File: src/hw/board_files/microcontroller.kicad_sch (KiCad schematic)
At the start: 15 parts, among them Q3 PMOS, Q4 NMOS, U6 ESP32-S3-WROOM-1, Y1 32.768kHz

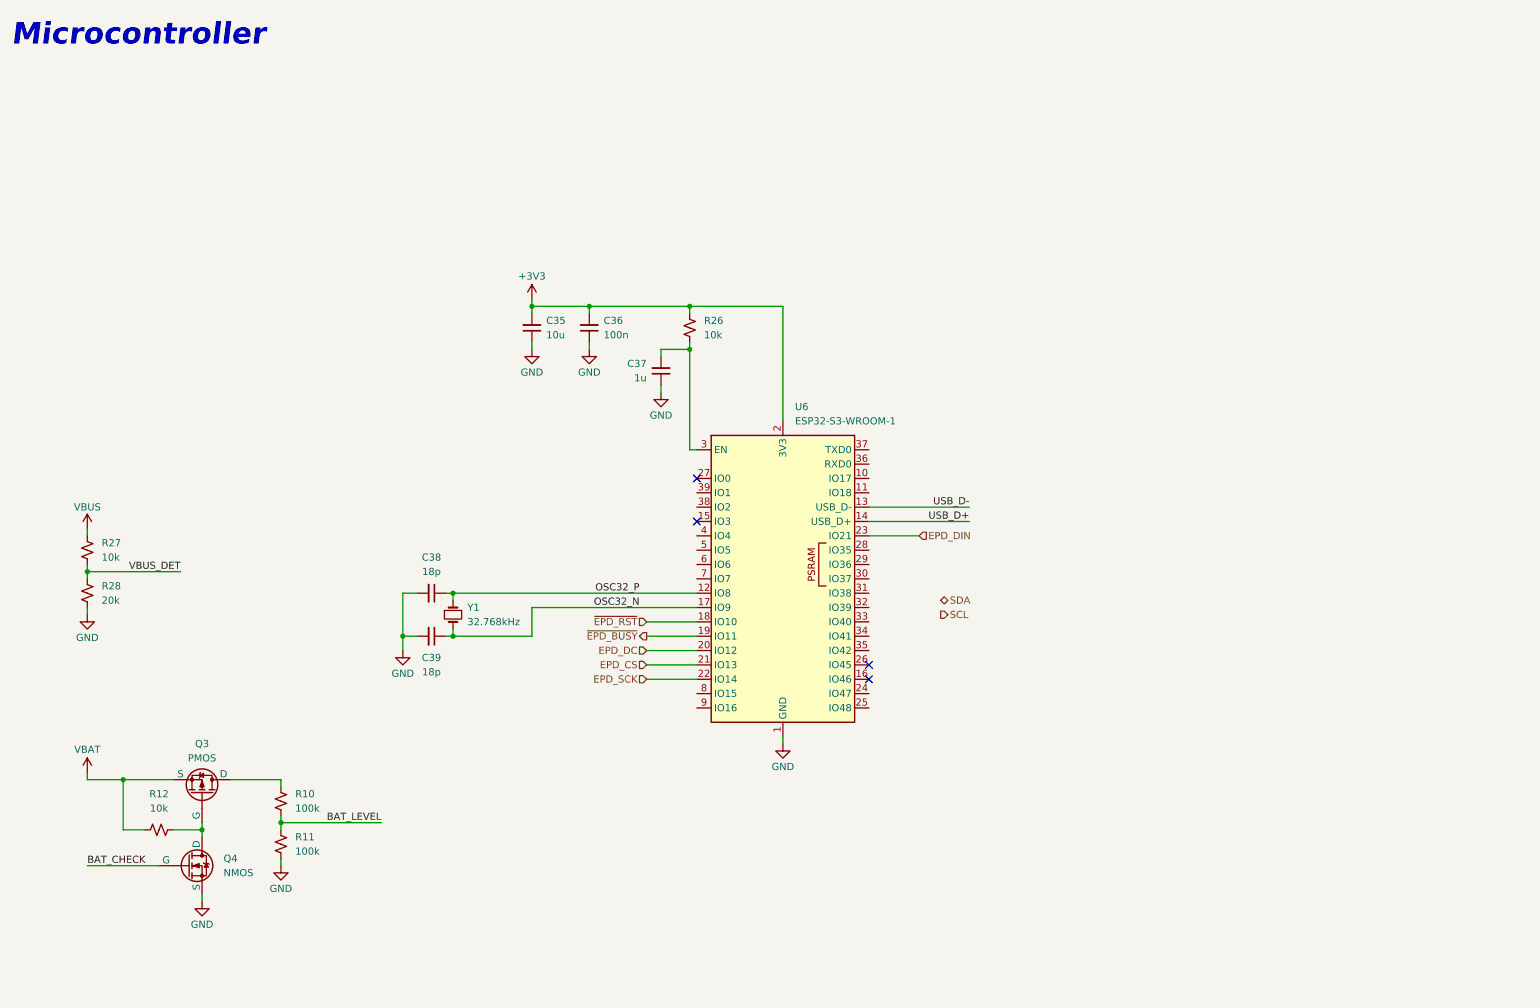
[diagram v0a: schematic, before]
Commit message: Schematic almost done. Assigning footprints
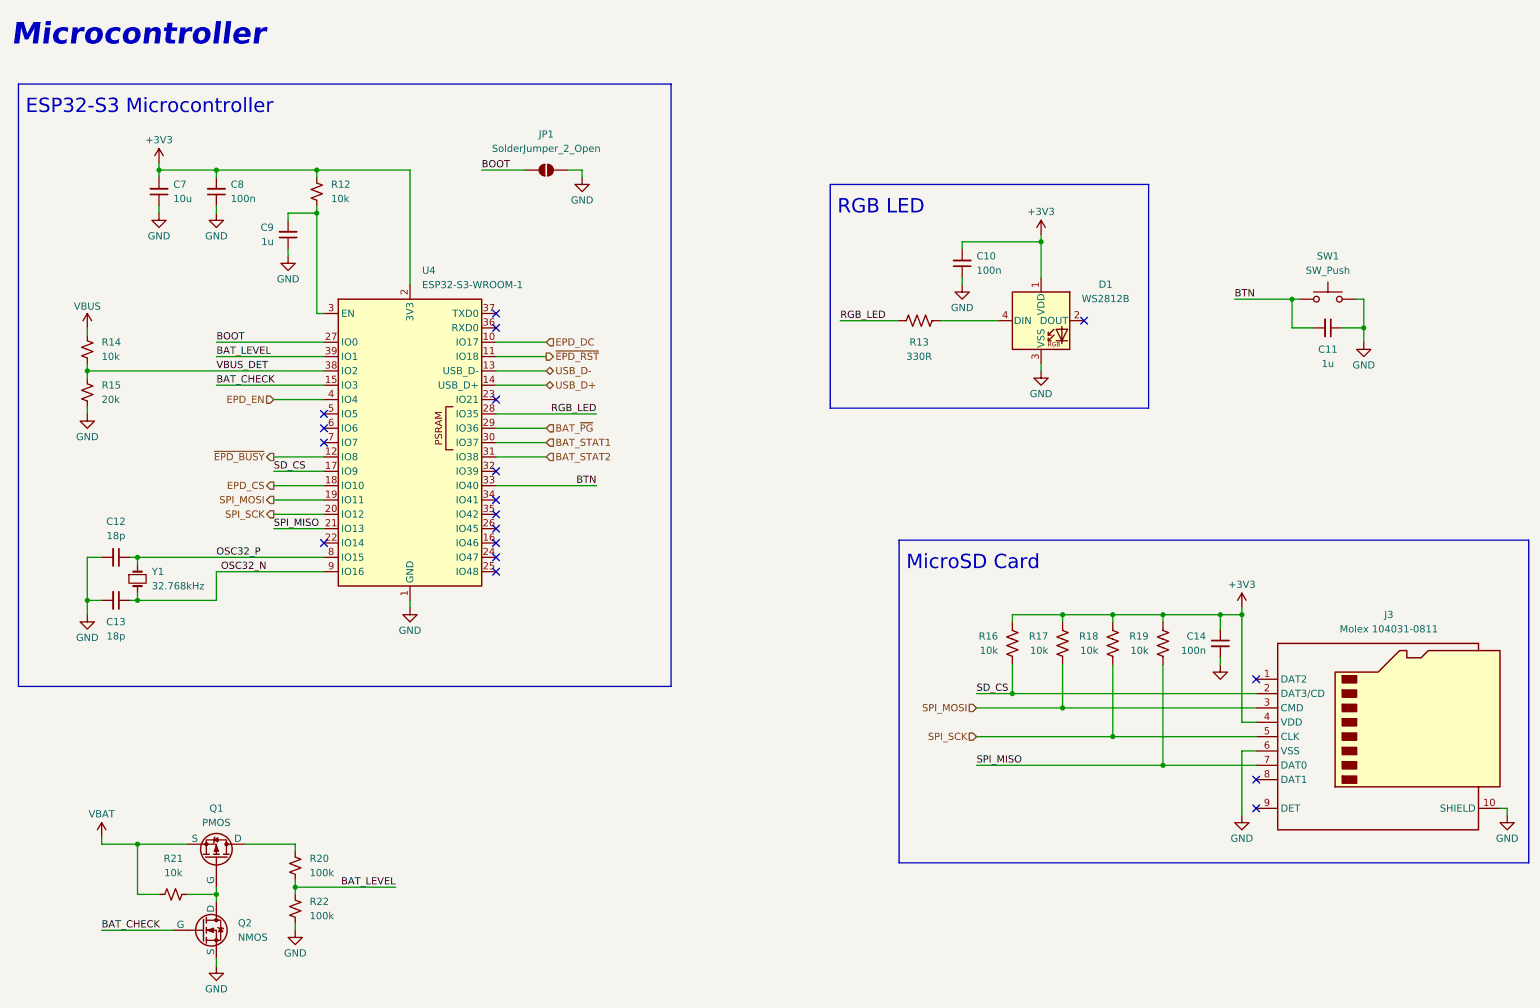
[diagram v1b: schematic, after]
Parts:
- added C10, C14: 100n, Capacitor_SMD:C_0603_1608Metric_Pad1.08x0.95mm_HandSolder, symbol Device:C_Small
- added C11: 1u, Capacitor_SMD:C_0603_1608Metric_Pad1.08x0.95mm_HandSolder, symbol Device:C_Small
- added D1: WS2812B, LED_SMD:LED_WS2812B_PLCC4_5.0x5.0mm_P3.2mm, symbol LED:WS2812B
- added J3: Molex 104031-0811, Connector_Card:microSD_HC_Molex_104031-0811, symbol Connector:Micro_SD_Card_Det1
- added JP1: SolderJumper_2_Open, Jumper:SolderJumper-2_P1.3mm_Open_RoundedPad1.0x1.5mm, symbol Jumper:SolderJumper_2_Open
- added R13: 330R, symbol Device:R_US
- added R16, R17, R18, R19: 10k, Resistor_SMD:R_0603_1608Metric_Pad0.98x0.95mm_HandSolder, symbol Device:R_US
- added SW1: SW_Push, Button_Switch_THT:SW_PUSH_6mm, symbol Switch:SW_Push
- renumbered C38 to C12, C39 to C13, C35 to C7, C36 to C8, C37 to C9, Q3 to Q1, Q4 to Q2, R26 to R12, R27 to R14, R28 to R15, R10 to R20, R12 to R21, R11 to R22, U6 to U4
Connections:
- net +3V3: now also C10.2, C14.1, D1.1 (VDD), J3.4 (VDD), R16.1, R17.1, R18.1, R19.1
- net BAT_CHECK: now also U4.15 (IO3)
- net BAT_LEVEL: now also U4.39 (IO1)
- net EPD_CS: now also U4.18 (IO10); no longer U4.21 (IO13)
- net EPD_DC: now also U4.10 (IO17); no longer U4.20 (IO12)
- net GND: now also C10.1, C11.1, C14.2, D1.3 (VSS), J3.10 (SHIELD), J3.6 (VSS), JP1.2 (B), SW1.2
- net OSC32_N: now also U4.9 (IO16); no longer U4.17 (IO9)
- net OSC32_P: now also U4.8 (IO15); no longer U4.12 (IO8)
- net VBUS_DET: now also U4.38 (IO2)
- net ~{EPD_BUSY}: now also U4.12 (IO8); no longer U4.19 (IO11)
- net ~{EPD_RST}: now also U4.11 (IO18); no longer U4.18 (IO10)
- net BOOT: now reaches U4.27 (IO0)
- net BOOT: now also JP1.1 (A)
- net RGB_LED: now reaches U4.28 (IO35)
- net RGB_LED: now also R13.1
- net BAT_~{PG}: now reaches U4.29 (IO36)
- net BAT_STAT1: now reaches U4.30 (IO37)
- net BAT_STAT2: now reaches U4.31 (IO38)
- net BTN: now reaches U4.33 (IO40)
- net BTN: now also C11.2, SW1.1
- net EPD_EN: now reaches U4.4 (IO4)
- net EPD_DIN: no longer names the net of U4.23 (IO21)
- net EPD_SCK: no longer names the net of U4.22 (IO14)
- new net: D1.4 (DIN), R13.2
- new net SD_CS: J3.2 (DAT3/CD), R16.2, U4.17 (IO9)
- new net SPI_MISO: J3.7 (DAT0), R19.2, U4.21 (IO13)
- new net SPI_MOSI: J3.3 (CMD), R17.2, U4.19 (IO11)
- new net SPI_SCK: J3.5 (CLK), R18.2, U4.20 (IO12)
- no-connect marks 4 -> 18
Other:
- note added: "ESP32-S3 Microcontroller"
- note added: "MicroSD Card"
- note added: "RGB LED"
- moved on the sheet: C12, C13, C7, C8, C9, Q1, Q2, R12, R14, R15, R20, R21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

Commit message: Schematic done. Started layout
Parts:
- removed Q1: PMOS, symbol Simulation_SPICE:PMOS
- removed Q2: NMOS, symbol Simulation_SPICE:NMOS
- added C12, C13: 1u, Capacitor_SMD:C_0603_1608Metric_Pad1.08x0.95mm_HandSolder, symbol Device:C_Small
- added C17: 100n, Capacitor_SMD:C_0603_1608Metric_Pad1.08x0.95mm_HandSolder, symbol Device:C_Small
- added J4: Conn_01x10, Connector_PinSocket_2.54mm:PinSocket_1x10_P2.54mm_Horizontal, symbol Connector_Generic:Conn_01x10
- added Q1: AO3401A, Package_TO_SOT_SMD:SOT-23, symbol Transistor_FET:AO3401A
- added Q2: BSS138, Package_TO_SOT_SMD:SOT-23, symbol Transistor_FET:BSS138
- added SW2, SW3: SW_Push, Button_Switch_THT:SW_PUSH_6mm, symbol Switch:SW_Push
- R12, R13, R14, R15, R21: footprint (none) -> Resistor_SMD:R_0603_1608Metric_Pad0.98x0.95mm_HandSolder
- R20, R22: footprint (none) -> Resistor_SMD:R_0805_2012Metric_Pad1.20x1.40mm_HandSolder
- renumbered C9 to C10, C10 to C11, C12 to C14, C13 to C15, C14 to C16, C11 to C9
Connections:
- net +3V3: now also J4.1 (Pin_1)
- net BAT_CHECK: now also Q2.1 (G)
- net EPD_CS: now also J4.6 (Pin_6)
- net GND: now also C12.1, C13.1, C17.1, J4.10 (Pin_10), Q2.2 (S), SW2.2, SW3.2
- net SD_CS: now also J4.5 (Pin_5)
- net SPI_MISO: now also J4.2 (Pin_2)
- net SPI_MOSI: now also J4.3 (Pin_3)
- net SPI_SCK: now also J4.4 (Pin_4)
- net VBAT: now also C17.2, Q1.2 (S)
- net GPIO41: now reaches U4.34 (IO41)
- net GPIO41: now also J4.8 (Pin_8)
- net GPIO42: now reaches U4.35 (IO42)
- net GPIO42: now also J4.9 (Pin_9)
- net BTN_1: now reaches U4.5 (IO5)
- net BTN_1: now also C9.2, SW1.1
- net BTN_2: now reaches U4.6 (IO6)
- net BTN_2: now also C12.2, SW2.1
- net BTN_3: now reaches U4.7 (IO7)
- net BTN_3: now also C13.2, SW3.1
- net at R20.1: now also Q1.3 (D)
- net at R21.2: now also Q1.1 (G), Q2.3 (D)
- removed net BTN: C9.2, SW1.1, U4.33 (IO40)
- new net GPIO40: J4.7 (Pin_7), U4.33 (IO40)
- no-connect marks 18 -> 13
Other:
- moved on the sheet: C9, SW1

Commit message: Laid out main components
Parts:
- J3: footprint Connector_Card:microSD_HC_Molex_104031-0811 -> Connector_Card:microSD_HC_Hirose_DM3D-SF
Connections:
- net BAT_STAT1: now also U4.24 (IO47); no longer U4.30 (IO37)
- net BAT_STAT2: now also U4.25 (IO48); no longer U4.31 (IO38)
- net BAT_~{PG}: now also U4.23 (IO21); no longer U4.29 (IO36)
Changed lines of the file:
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@@
-	)
-	(no_connect
-		(at 99.06 111.76)
-	)
-	(no_connect
-		(at 99.06 81.28)
-	)
-	(no_connect
-		(at 99.06 109.22)
 	)
 	(no_connect
@@
 		(at 203.2 67.31)
 	)
+	(no_connect
+		(at 99.06 86.36)
+	)
+	(no_connect
+		(at 99.06 91.44)
+	)
+	(no_connect
+		(at 99.06 88.9)
+	)
 	(wire
 		(pts
@@
 	(wire
 		(pts
-			(xy 107.95 91.44) (xy 99.06 91.44)
+			(xy 107.95 111.76) (xy 99.06 111.76)
 		)
 		(stroke
@@
 	(wire
 		(pts
-			(xy 107.95 86.36) (xy 99.06 86.36)
+			(xy 107.95 81.28) (xy 99.06 81.28)
 		)
 		(stroke
@@
 	(wire
 		(pts
-			(xy 107.95 88.9) (xy 99.06 88.9)
+			(xy 107.95 109.22) (xy 99.06 109.22)
 		)
 		(stroke
@@
 	(hierarchical_label "BAT_STAT1"
 		(shape input)
-		(at 107.95 88.9 0)
+		(at 107.95 109.22 0)
 		(effects
 			(font
@@
 	(hierarchical_label "BAT_~{PG}"
 		(shape input)
-		(at 107.95 86.36 0)
+		(at 107.95 81.28 0)
 		(effects
 			(font
@@
 	(hierarchical_label "BAT_STAT2"
 		(shape input)
-		(at 107.95 91.44 0)
+		(at 107.95 111.76 0)
 		(effects
 			(font
@@
 			)
 		)
-		(property "Footprint" "Connector_Card:microSD_HC_Molex_104031-0811"
+		(property "Footprint" "Connector_Card:microSD_HC_Hirose_DM3D-SF"
 			(at 308.61 123.19 0)
 			(effects
@@
 		(on_board yes)
 		(dnp no)
-		(fields_autoplaced yes)
 		(property "Reference" "U4"
 			(at 85.9633 58.42 0)
